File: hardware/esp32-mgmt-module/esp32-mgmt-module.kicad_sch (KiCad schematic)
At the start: 90 parts, among them J1 Bus_PCI_Express_x1, J2 BOOT, J3 RJ45_Hanrun_HR913550A_Horizon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, J4 GPIO, J5 SWD, J6 USB_C, J7 UART, Q1 MMBT3904, Q2 MMBT3904, SW1 RESET, U1 RTL8201F-VB-CG, U2 74LVC1G14, U3 AMS1117-3.3, U4 ESP32-WROOM-32E, U5 CH9102F, Y1 50MHz

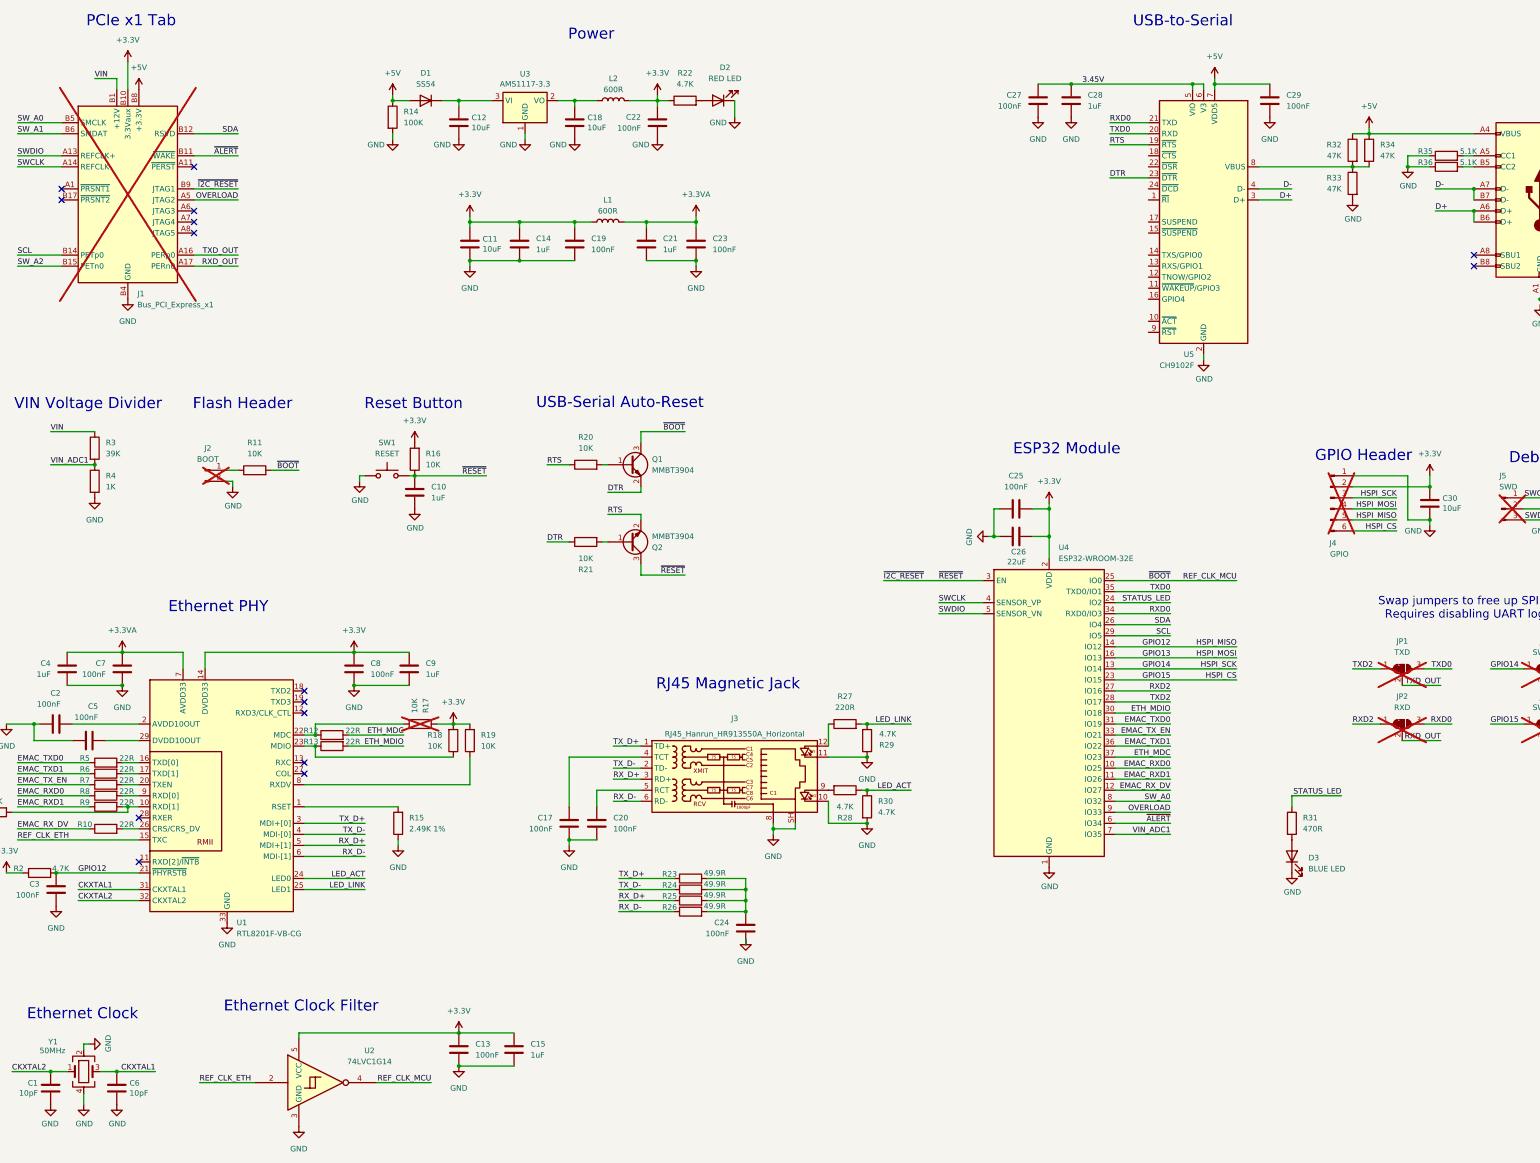
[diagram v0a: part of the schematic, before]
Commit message: fix: make ethernet functional
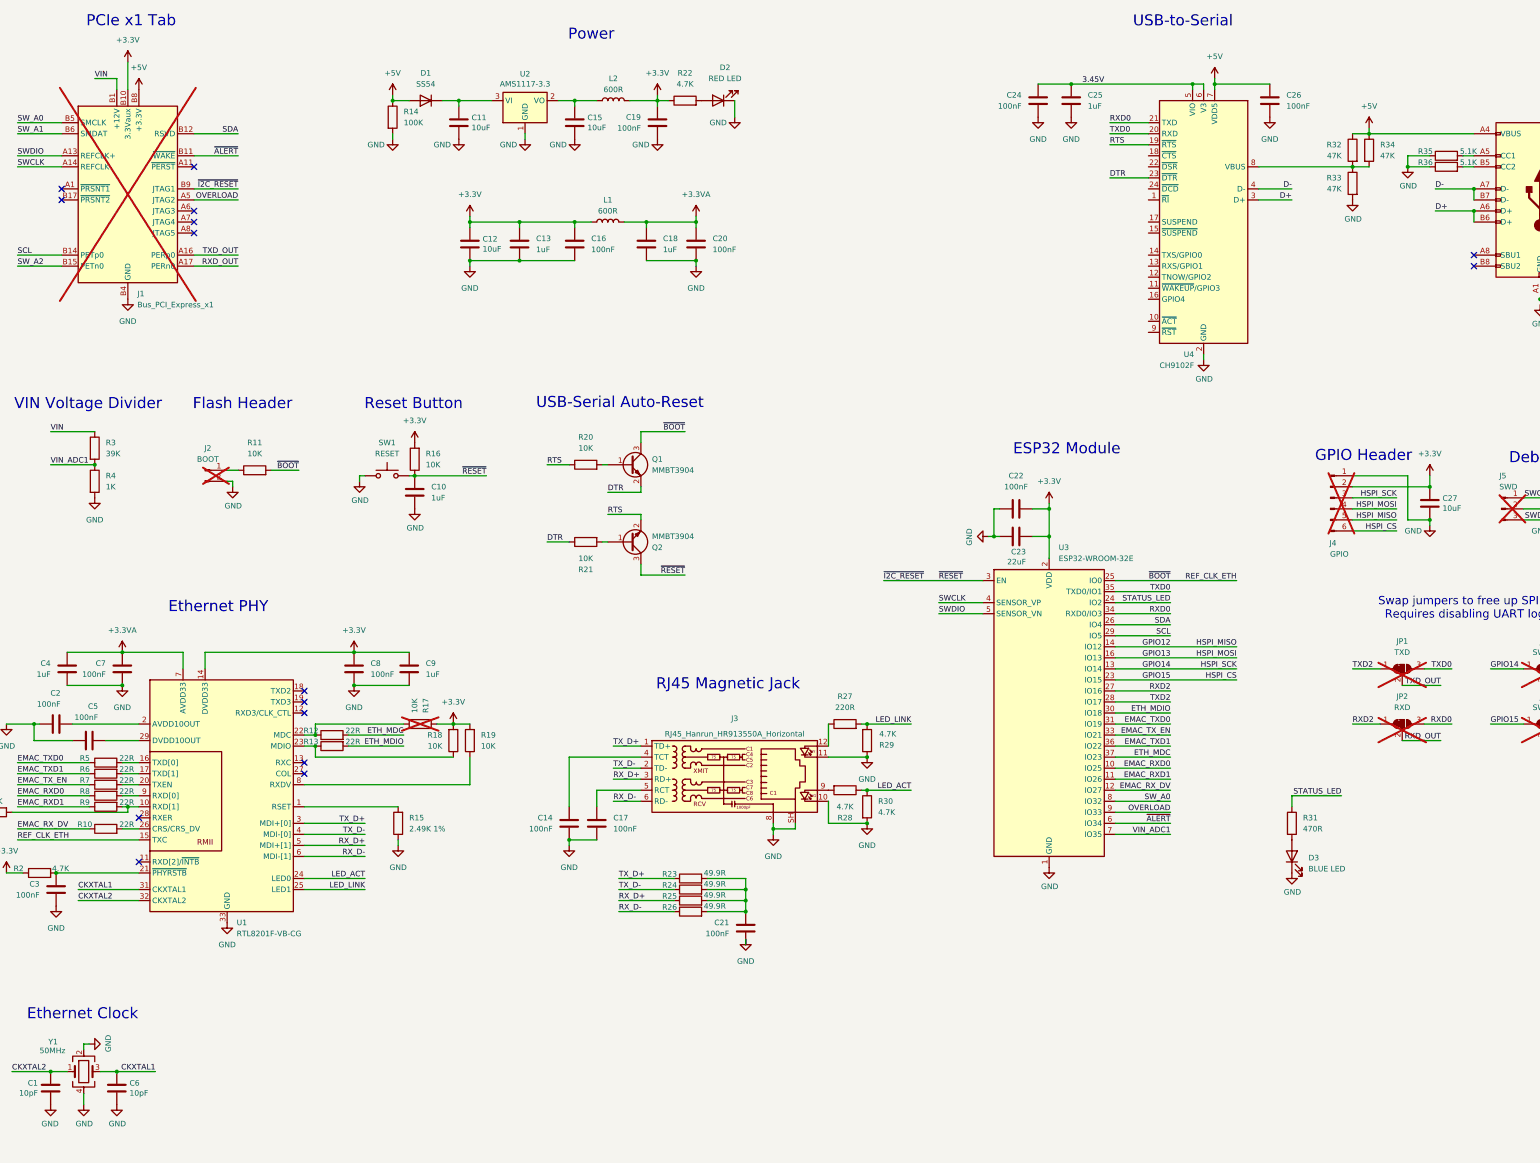
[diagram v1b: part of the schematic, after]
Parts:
- removed C13: 100nF, Capacitor_SMD:C_0402_1005Metric, symbol Device:C
- removed C15: 1uF, Capacitor_SMD:C_0402_1005Metric, symbol Device:C
- removed U2: 74LVC1G14, Package_TO_SOT_SMD:SOT-353_SC-70-5, symbol 74xGxx:74LVC1G14
- renumbered C12 to C11, C11 to C12, C14 to C13, C17 to C14, C18 to C15, C19 to C16, C20 to C17, C21 to C18, C22 to C19, C23 to C20, C24 to C21, C25 to C22, C26 to C23, C27 to C24, C28 to C25, C29 to C26, C30 to C27, U3 to U2, U4 to U3, U5 to U4
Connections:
- net REF_CLK_MCU is gone; now on net REF_CLK_ETH: Q1.3 (C), R11.2, U3.25 (IO0)
- net GPIO12: no longer C3.1, R2.2, U1.21 (~{PHYRSTB})
- new net: C3.1, R2.2, U1.21 (~{PHYRSTB})
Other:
- note removed: "Ethernet Clock Filter"
